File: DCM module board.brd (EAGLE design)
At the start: 130 x 111 mm, 21 parts, among them X1 5566-10

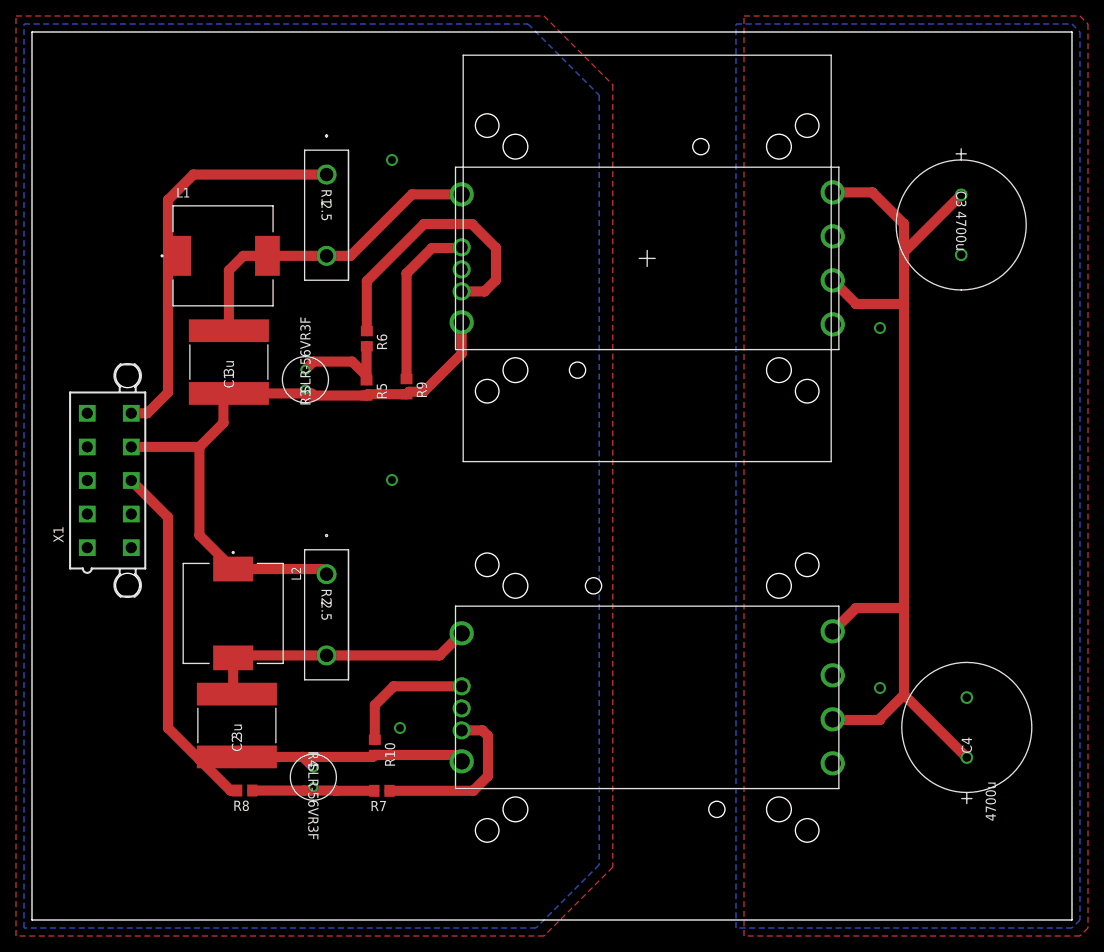
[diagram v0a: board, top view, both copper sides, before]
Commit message: Add files via upload
Version 1.1
- Modified power planes for high-voltage side.
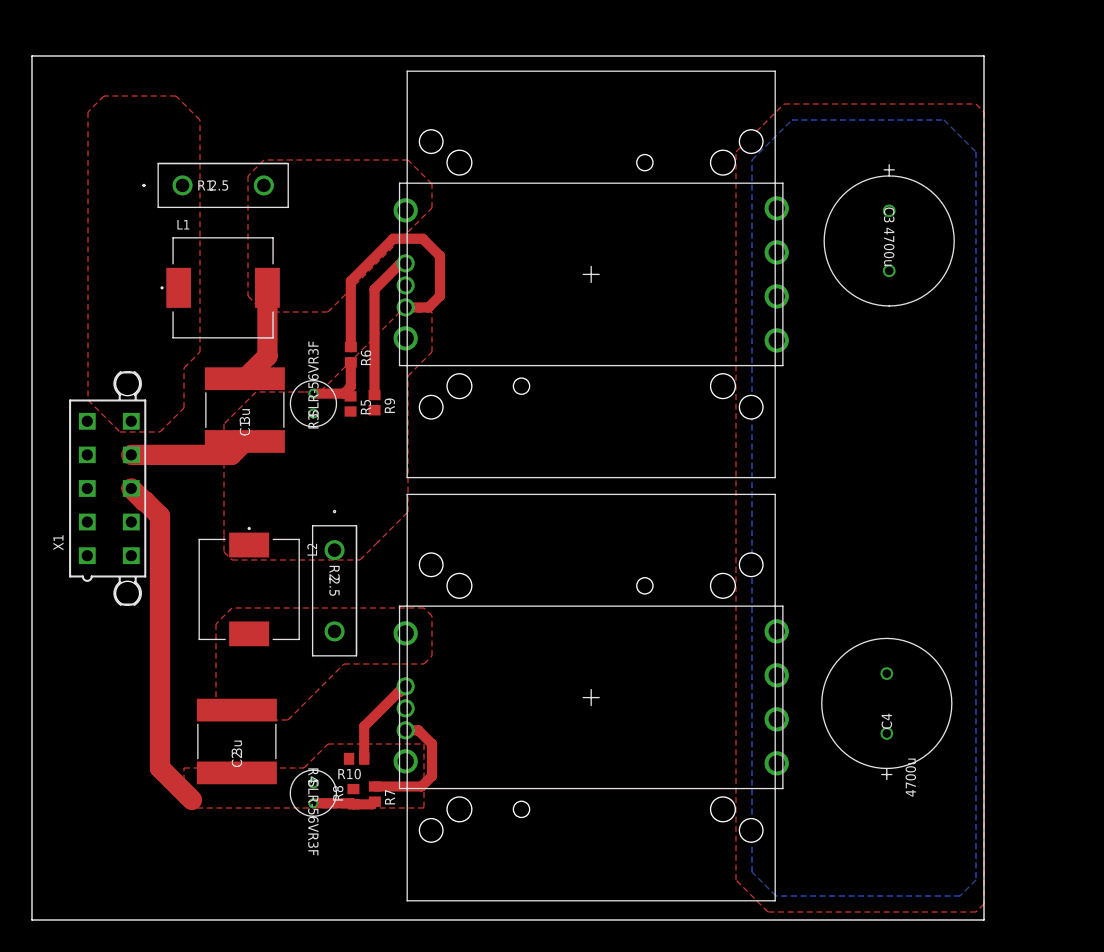
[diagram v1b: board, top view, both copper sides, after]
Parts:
- moved R1 18.1 mm to (18.8, 91.8), turned to 0 degrees
- moved R8 13.6 mm to (40.2, 15.4), turned to 90 degrees
- moved C4 10.4 mm to (106.8, 23.3)
- moved C3 9.22 mm to (107.2, 88.6)
- moved U$1 7.28 mm to (69.9, 80.7)
- moved U$4 7.28 mm to (69.9, 80.7)
- moved U$2 7.00 mm to (69.9, 27.8)
- moved U$3 7.00 mm to (69.9, 27.8), flipped to the top
- moved C1 6.32 mm to (26.6, 63.7)
- moved R9 4.47 mm to (42.8, 64.7)
- moved L1 4.00 mm to (23.9, 79.0)
- moved L2 3.61 mm to (27.1, 41.3)
- moved R2 3.16 mm to (37.8, 46.2)
- moved R3 3.16 mm to (35.2, 65.8)
- moved R5 2.83 mm to (39.8, 64.5)
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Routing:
- net N$3: track 121.2 -> 0.00 mm
- net 250V: track 82.7 -> 14.9 mm
- net 500V: track 52.2 -> 0.00 mm
- net 0V: track 79.9 -> 42.2 mm
- net N$4: track 34.6 -> 0.00 mm
- net N$1: track 40.6 -> 12.5 mm
- net N$9: track 15.8 -> 7.87 mm
- net FT2: track 21.7 -> 15.7 mm
- net TR2: track 16.2 -> 11.3 mm
- net N$6: track 13.1 -> 9.04 mm
- net FT1: track 35.5 -> 32.4 mm
- net TR1: track 21.4 -> 18.4 mm
- added copper zone on layer 1, net 0V
- added copper zone on layer 1, net 250V
- added copper zone on layer 1, net 500V
- added copper zone on layer 1, net N$1
- added copper zone on layer 1, net N$3
- added copper zone on layer 1, net N$4
- removed copper zone on layer 1, net GND
- removed copper zone on layer 16, net GND3
- removed copper zone on layer 1, net GND7
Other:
- board size 130 x 111 mm -> 119 x 108 mm
